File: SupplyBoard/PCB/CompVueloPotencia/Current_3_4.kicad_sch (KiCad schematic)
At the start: 0 parts

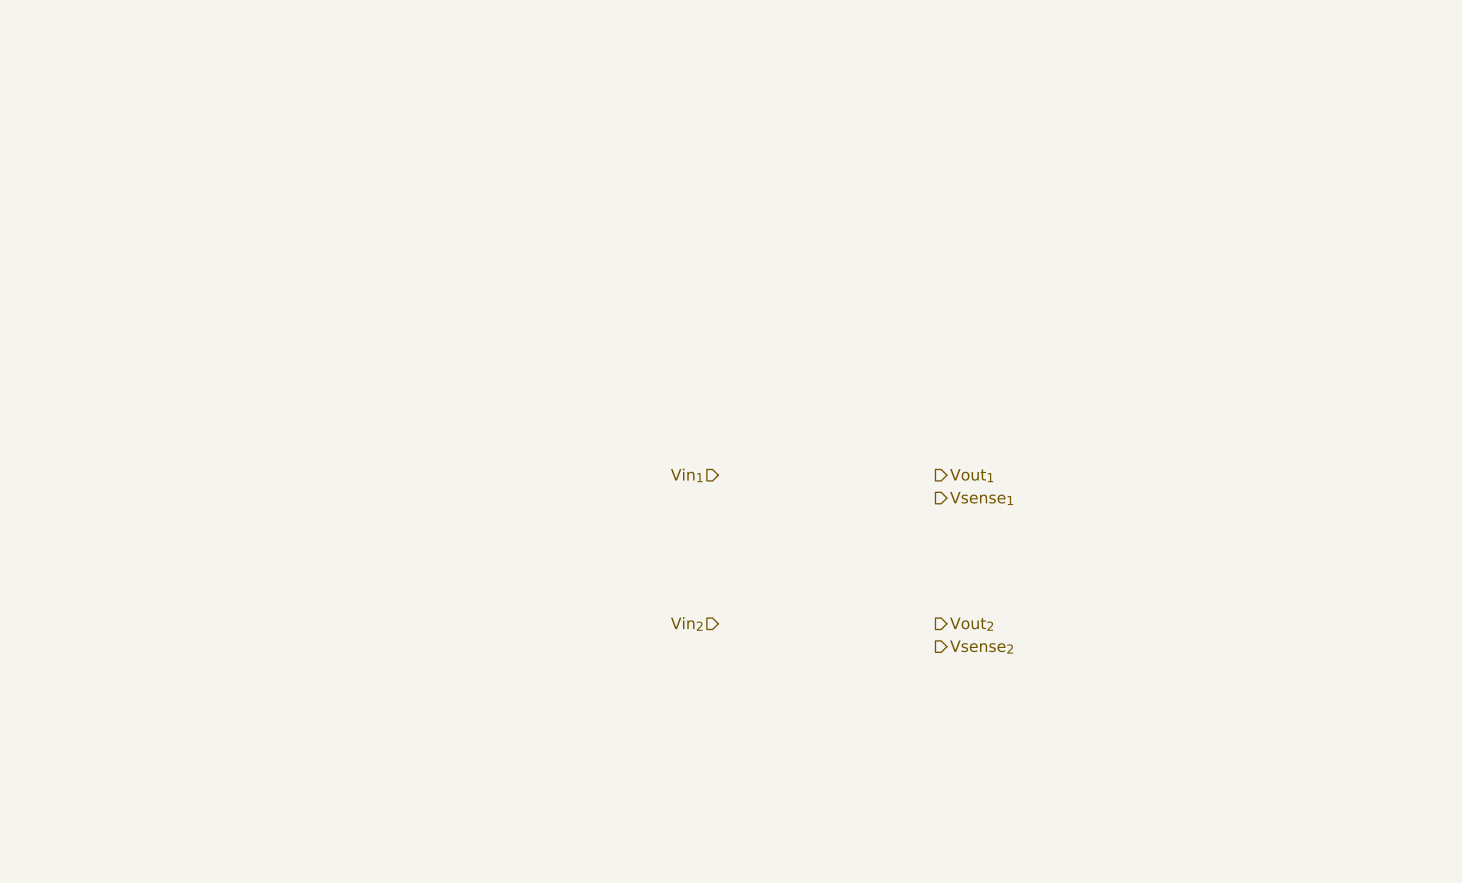
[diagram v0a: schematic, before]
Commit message: SupplyBoard - finish current sense
Finish the Current Sensor Circuit and add more 3.3V out, i change de microcontroles to a mcu that have the exact GPIO's
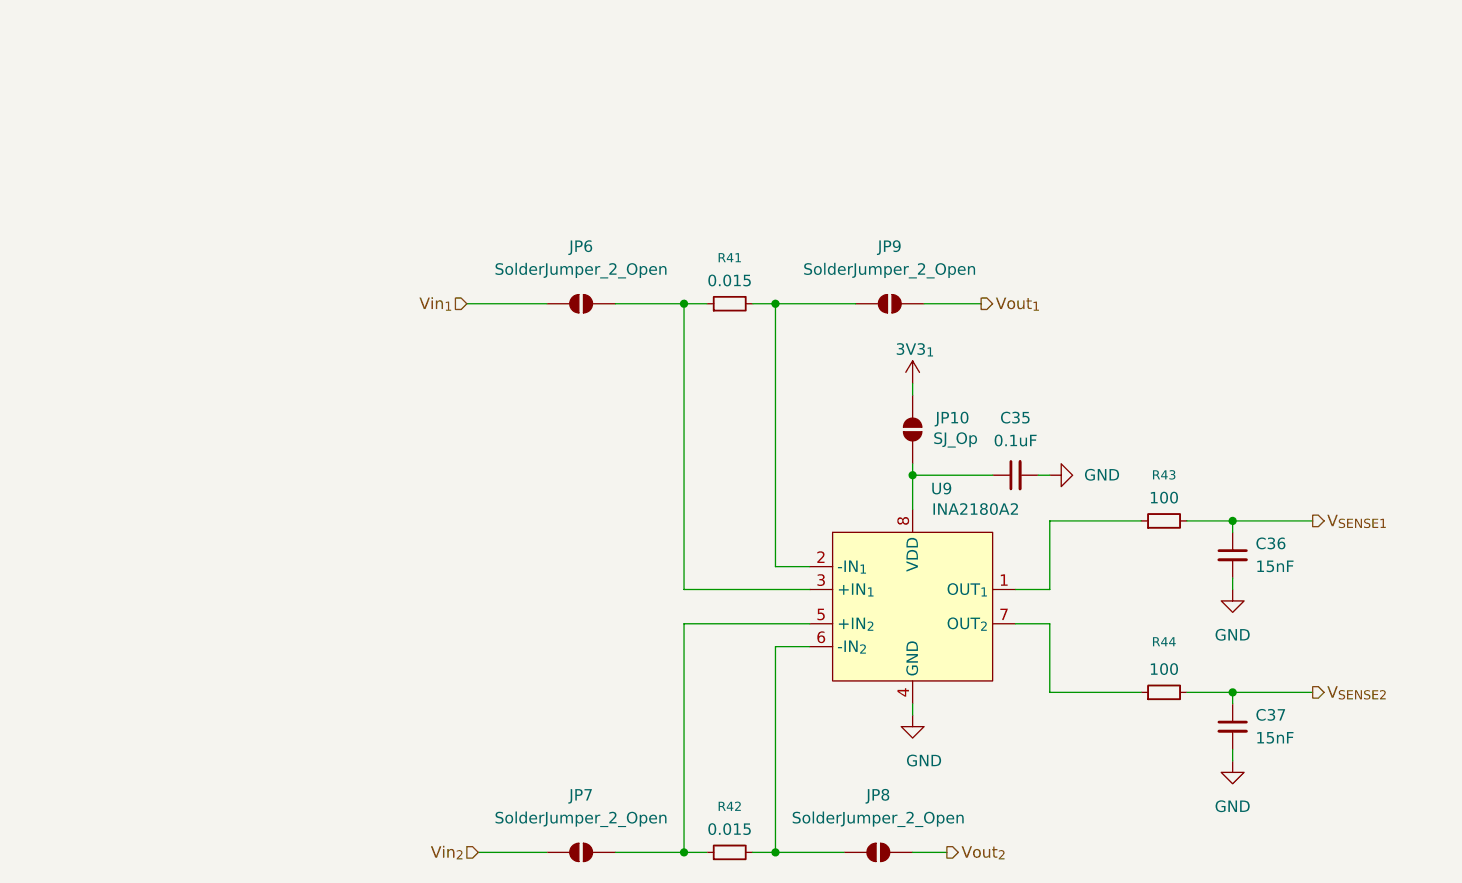
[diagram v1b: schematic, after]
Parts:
- added C35: 0.1uF, symbol Device:C_Small
- added C36, C37: 15nF, symbol Device:C_Small
- added JP10: SJ_Op, Jumper:SolderJumper-2_P1.3mm_Open_RoundedPad1.0x1.5mm, symbol Jumper:SolderJumper_2_Open
- added JP6, JP7, JP8, JP9: SolderJumper_2_Open, Jumper:SolderJumper-2_P1.3mm_Open_RoundedPad1.0x1.5mm, symbol Jumper:SolderJumper_2_Open
- added R41, R42: 0.015, Resistor_SMD:R_1206_3216Metric_Pad1.30x1.75mm_HandSolder, symbol Device:R_Small
- added R43, R44: 100, symbol Device:R_Small
- added U9: INA2180A2, Package_SO:Texas_S-PDSO-G8_3x3mm_P0.65mm, symbol CompVuelo:INA2180
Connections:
- net Vin_{1}: now also JP6.1 (A)
- net Vin_{2}: now also JP7.1 (A)
- net Vout_{1}: now also JP9.2 (B)
- net Vout_{2}: now also JP8.2 (B)
- new net: JP6.2 (B), R41.1, U9.3 (+IN_{1})
- new net: R43.1, U9.1 (OUT_{1})
- new net: JP9.1 (A), R41.2, U9.2 (-IN_{1})
- new net: JP7.2 (B), R42.1, U9.5 (+IN_{2})
- new net: JP8.1 (A), R42.2, U9.6 (-IN_{2})
- new net: R44.1, U9.7 (OUT_{2})
- new net: C35.1, JP10.1 (A), U9.8 (VDD)
- new net 3V3_{1}: JP10.2 (B)
- new net GND: C35.2, C36.2, C37.2, U9.4 (GND)
- new net V_{SENSE1}: C36.1, R43.2
- new net V_{SENSE2}: C37.1, R44.2

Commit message: SupplyBoard - update layout
schematic completed and PCB layout started; only the routing of the traces remains to be done
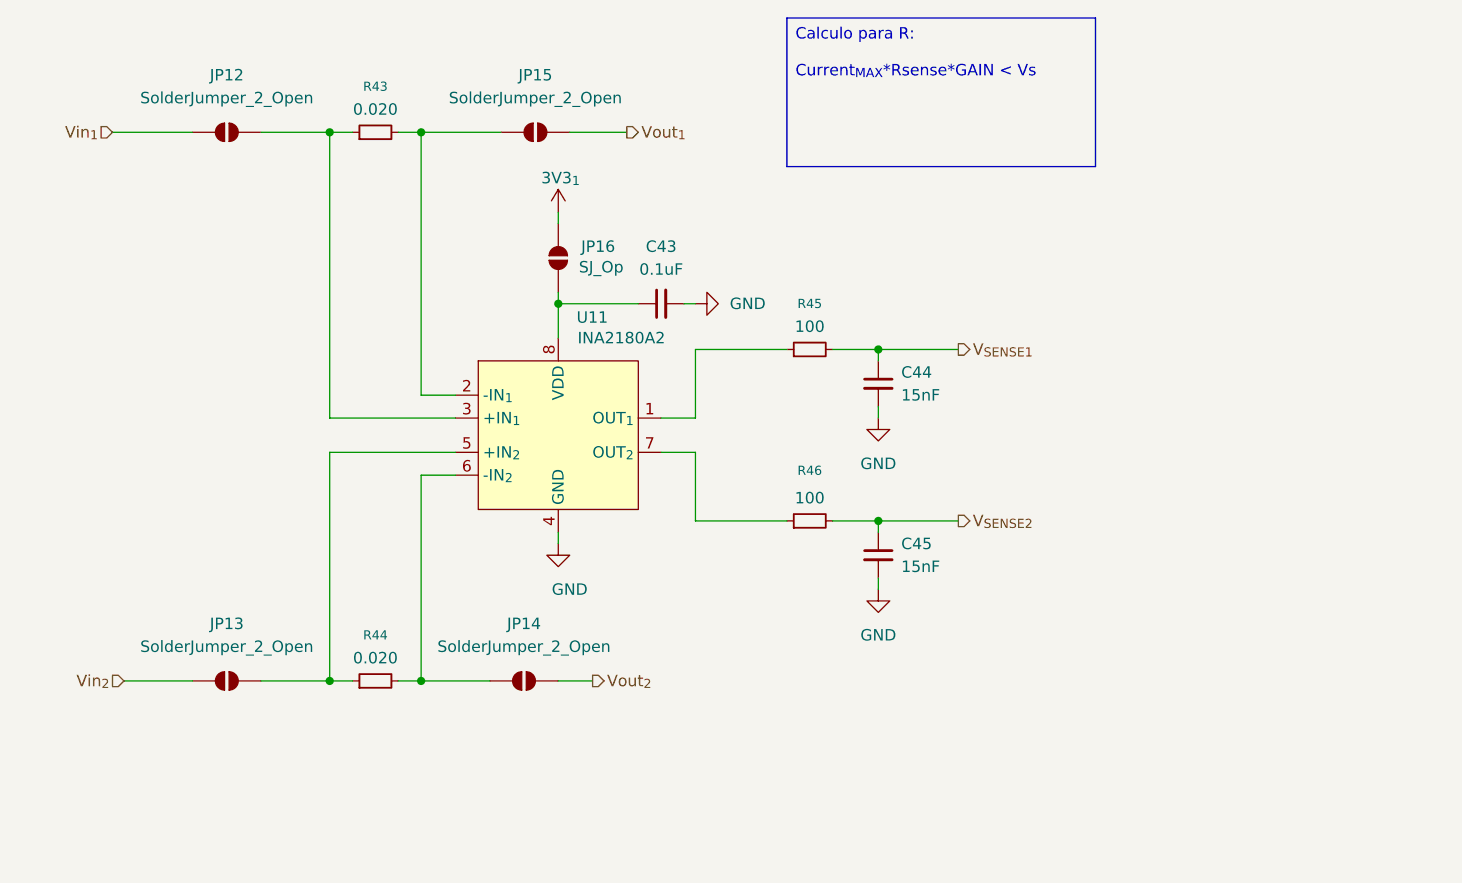
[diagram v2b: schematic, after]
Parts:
- C43: renamed from C35; footprint (none) -> Capacitor_SMD:C_0805_2012Metric_Pad1.18x1.45mm_HandSolder
- C44: renamed from C36; footprint (none) -> Capacitor_SMD:C_0805_2012Metric_Pad1.18x1.45mm_HandSolder
- C45: renamed from C37; footprint (none) -> Capacitor_SMD:C_0805_2012Metric_Pad1.18x1.45mm_HandSolder
- R43: renamed from R41; value 0.015 -> 0.020
- R44: renamed from R42; value 0.015 -> 0.020
- R45: renamed from R43; footprint (none) -> Resistor_SMD:R_0805_2012Metric_Pad1.20x1.40mm_HandSolder
- R46: renamed from R44; footprint (none) -> Resistor_SMD:R_0805_2012Metric_Pad1.20x1.40mm_HandSolder
- U11: renamed from U9; footprint Package_SO:Texas_S-PDSO-G8_3x3mm_P0.65mm -> CompVuelo:Texas_S-PDSO-G8_3x3mm_P0.65mm
- renumbered JP6 to JP12, JP7 to JP13, JP8 to JP14, JP9 to JP15, JP10 to JP16
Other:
- moved on the sheet: C43, C44, C45, JP12, JP13, JP14, JP15, JP16, R43, R44, R45, R46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
